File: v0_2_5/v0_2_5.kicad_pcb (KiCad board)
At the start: 2 copper layers, 91.4 x 50.8 mm, 58 parts, among them IC1 RASPBERRY_PI_PICO_W, IC2 BH1750FVI-TR, IC3 AP2138N-3.3TRG1, J1 S2B-PH-SM4-TB_LF__SN_, J2 HYCW110-TF10-180B, J4 SM04B-SRSS-TB, J5 Screw_Terminal_01x03, J6 Conn_01x02_Pin, Q1 DMG2301L-7, Q2 DMG2301L-7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

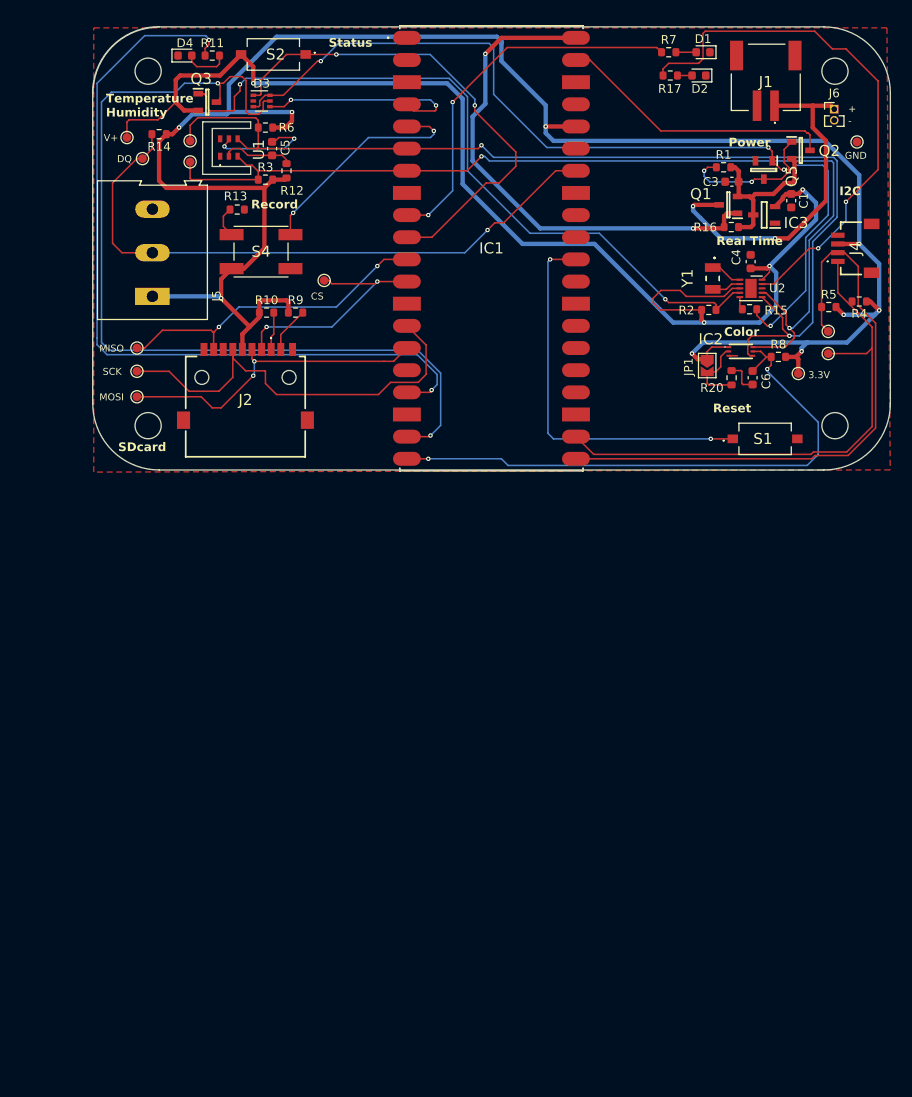
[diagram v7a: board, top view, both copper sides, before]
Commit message: replace sdcard
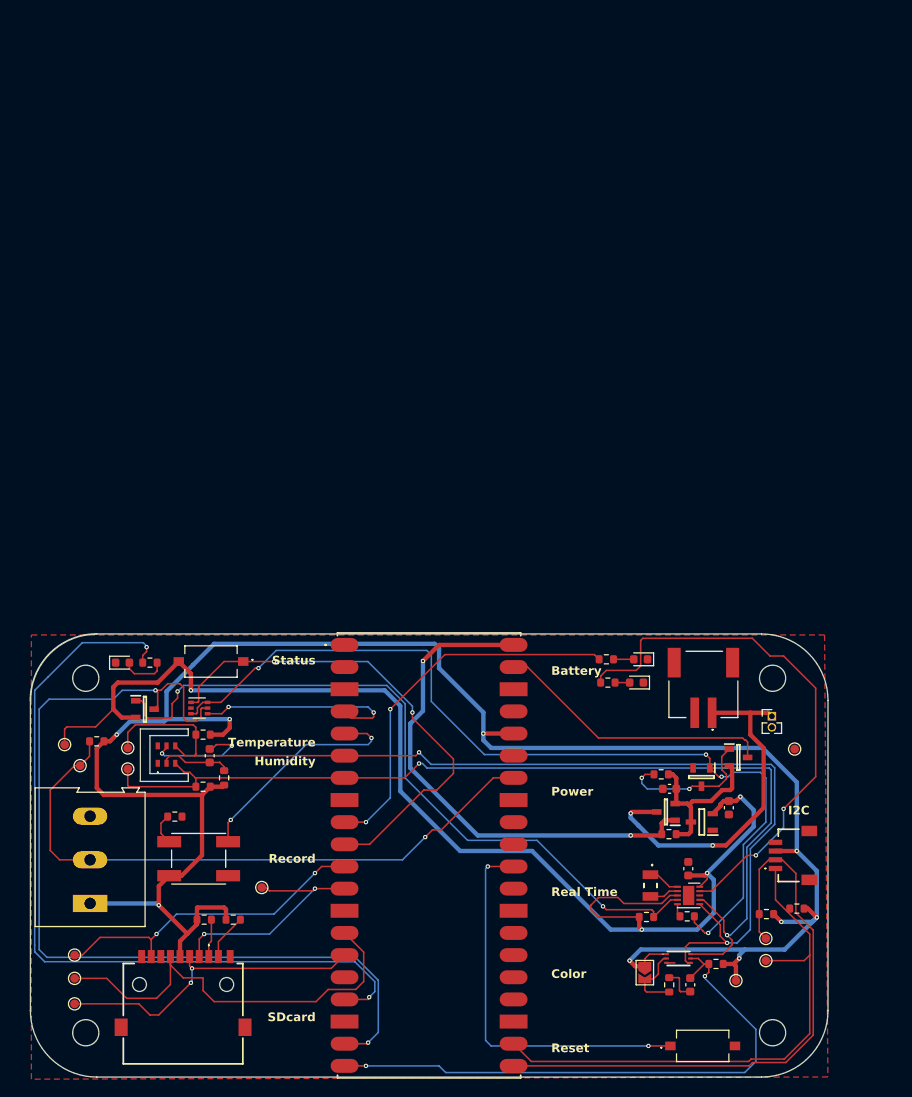
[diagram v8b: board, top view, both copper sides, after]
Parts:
- moved C1 70.0 mm to (180.5, 91.8)
- moved C4 70.0 mm to (175.9, 98.8)
- moved C5 70.0 mm to (121.0, 85.8)
- moved D2 70.0 mm to (170.0, 77.4)
- moved D3 70.0 mm to (119.8, 80.4)
- moved D4 70.0 mm to (111.0, 75.1)
- moved IC1 70.0 mm to (146.2, 97.2)
- moved IC2 70.0 mm to (174.8, 109.1)
- moved IC3 70.0 mm to (177.4, 93.4)
- moved J1 70.0 mm to (177.6, 77.6)
- moved J2 70.0 mm to (118.0, 115.4)
- moved J4 70.0 mm to (188.2, 97.2)
- moved J5 70.0 mm to (107.3, 102.8)
- moved J6 70.0 mm to (185.5, 81.3)
- moved JP1 70.0 mm to (170.9, 110.7)
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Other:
- outline, holes or cut-outs redrawn
- board text added: "Battery"
- board text added: "Humidity"
- board text added: "SCL"
- board text added: "SDA"
- board text added: "Temperature"
- board text removed: "Temperature Humidity"
